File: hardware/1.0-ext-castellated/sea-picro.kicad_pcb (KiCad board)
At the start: 4 copper layers, 17.8 x 33 mm, 54 parts, among them J1 USB_C_Receptacle_USB2.0, J2 Sea-Picro, Q1 2N7002VC-7, Q2 2N7002VC-7, U1 XC6210B332MR-G, U2 GD25Q64CWIGR, U3 RP2040, U4 74LVC1T45, Y1 12MHz

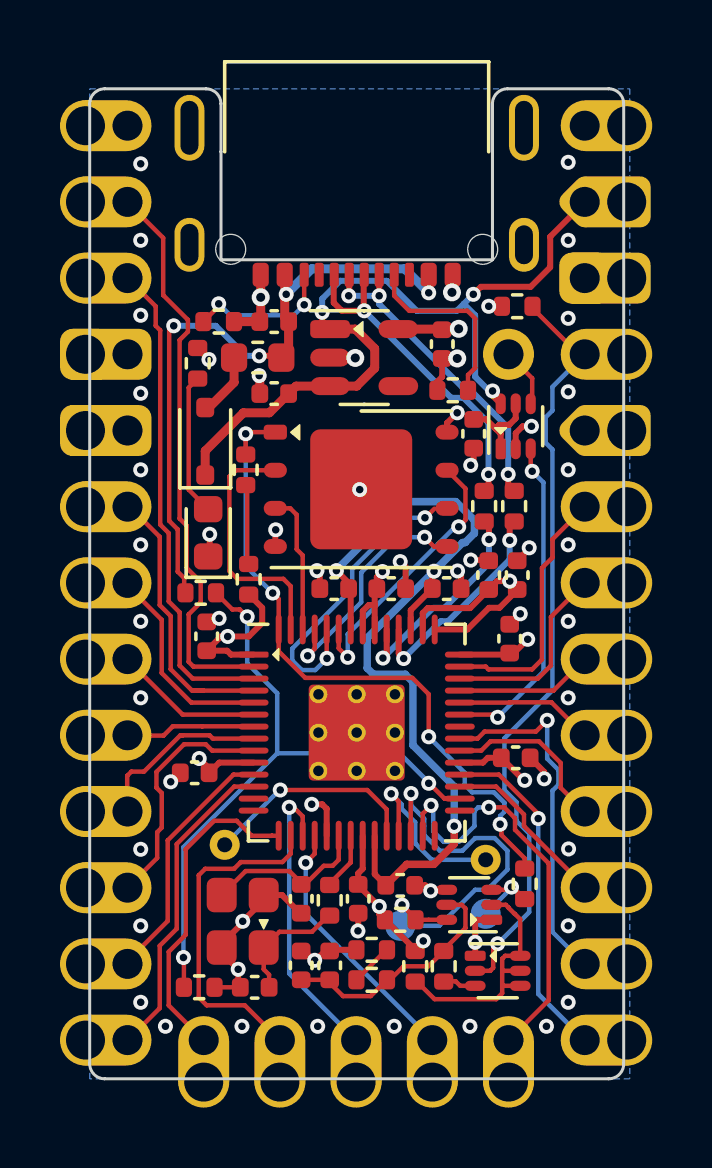
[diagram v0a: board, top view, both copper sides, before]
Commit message: fix trace width for level shifter
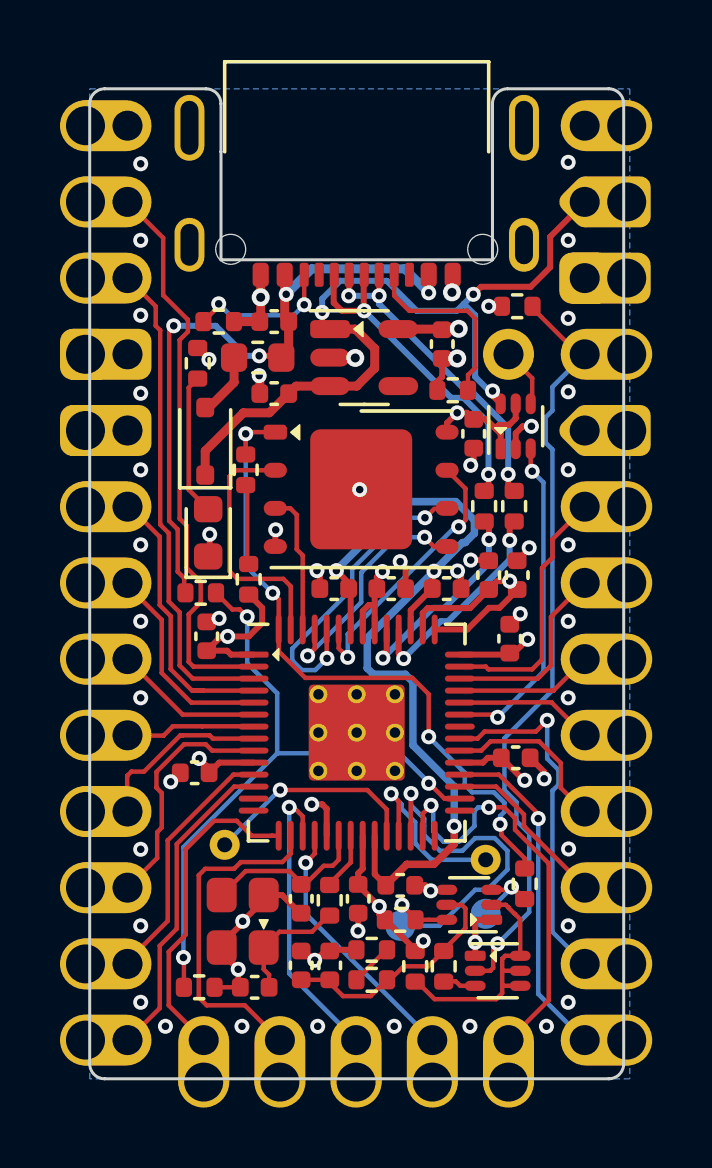
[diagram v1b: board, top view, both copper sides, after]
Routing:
- net +3V3: track 34.8 -> 35.4 mm
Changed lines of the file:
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@@
   (segment (start 130.6 91.49) (end 130.88 91.21) (width 0.2) (layer "F.Cu") (net 7))
   (segment (start 129.6375 97.26) (end 130.41 97.26) (width 0.2) (layer "F.Cu") (net 7))
+  (segment (start 129.88 85.6) (end 130.1 85.82) (width 0.2) (layer "F.Cu") (net 7))
   (segment (start 131.3 93.61) (end 131.44 93.61) (width 0.2) (layer "F.Cu") (net 7))
   (segment (start 121.2 93.53) (end 121.674421 93.055579) (width 0.2) (layer "F.Cu") (net 7))
@@
   (segment (start 131.44 93.61) (end 131.9 93.15) (width 0.2) (layer "F.Cu") (net 7))
   (segment (start 129.98 92.11) (end 130.6 91.49) (width 0.2) (layer "F.Cu") (net 7))
+  (segment (start 129.55 85.6) (end 129.88 85.6) (width 0.2) (layer "F.Cu") (net 7))
   (segment (start 126.952589 102.053918) (end 126.952589 102.312589) (width 0.2) (layer "F.Cu") (net 7))
   (segment (start 131.286695 86) (end 130.95 86) (width 0.2) (layer "F.Cu") (net 7))
